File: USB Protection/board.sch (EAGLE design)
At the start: 6 parts

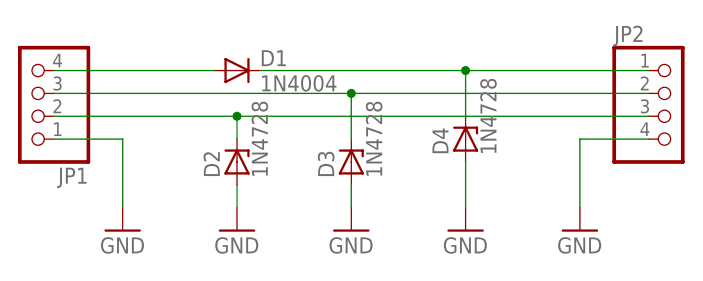
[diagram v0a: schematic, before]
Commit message: Removed power zener diode
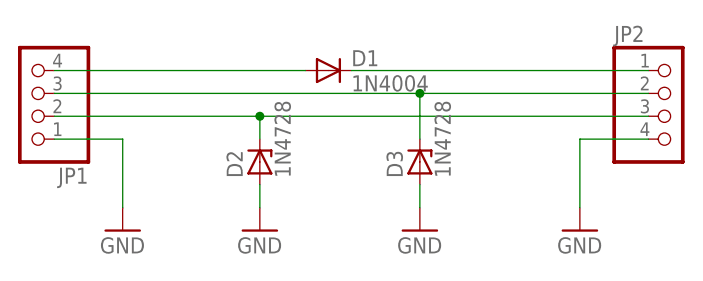
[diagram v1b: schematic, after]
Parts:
- removed D4: 1N4728, diode:1N4728
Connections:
- net GND: no longer D4.A
- net N$2: no longer D4.C
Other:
- moved on the sheet: D1, D2, D3
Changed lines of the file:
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@@
 <part name="D2" library="diode" library_urn="urn:adsk.eagle:library:210" deviceset="1N4728" device="" package3d_urn="urn:adsk.eagle:package:43341/1"/>
 <part name="D3" library="diode" library_urn="urn:adsk.eagle:library:210" deviceset="1N4728" device="" package3d_urn="urn:adsk.eagle:package:43341/1"/>
-<part name="D4" library="diode" library_urn="urn:adsk.eagle:library:210" deviceset="1N4728" device="" package3d_urn="urn:adsk.eagle:package:43341/1"/>
 <part name="JP1" library="pinhead" library_urn="urn:adsk.eagle:library:325" deviceset="PINHD-1X4" device="" package3d_urn="urn:adsk.eagle:package:22407/2"/>
 <part name="JP2" library="pinhead" library_urn="urn:adsk.eagle:library:325" deviceset="PINHD-1X4" device="" package3d_urn="urn:adsk.eagle:package:22407/2"/>
 <part name="GND1" library="supply1" library_urn="urn:adsk.eagle:library:371" deviceset="GND" device=""/>
-<part name="GND2" library="supply1" library_urn="urn:adsk.eagle:library:371" deviceset="GND" device=""/>
 <part name="GND3" library="supply1" library_urn="urn:adsk.eagle:library:371" deviceset="GND" device=""/>
 <part name="GND4" library="supply1" library_urn="urn:adsk.eagle:library:371" deviceset="GND" device=""/>
@@
 </plain>
 <instances>
-<instance part="D1" gate="1" x="10.16" y="55.88"/>
-<instance part="D2" gate="1" x="10.16" y="45.72" rot="R90"/>
-<instance part="D3" gate="1" x="22.86" y="45.72" rot="R90"/>
-<instance part="D4" gate="1" x="35.56" y="48.26" rot="R90"/>
+<instance part="D1" gate="1" x="20.32" y="55.88"/>
+<instance part="D2" gate="1" x="12.7" y="45.72" rot="R90"/>
+<instance part="D3" gate="1" x="30.48" y="45.72" rot="R90"/>
 <instance part="JP1" gate="A" x="-12.7" y="53.34" rot="R180"/>
 <instance part="JP2" gate="A" x="58.42" y="50.8"/>
 <instance part="GND1" gate="1" x="48.26" y="38.1"/>
-<instance part="GND2" gate="1" x="35.56" y="38.1"/>
 <instance part="GND3" gate="1" x="-2.54" y="38.1"/>
-<instance part="GND4" gate="1" x="22.86" y="38.1"/>
-<instance part="GND5" gate="1" x="10.16" y="38.1"/>
+<instance part="GND4" gate="1" x="30.48" y="38.1"/>
+<instance part="GND5" gate="1" x="12.7" y="38.1"/>
 </instances>
 <busses>
@@
 <pinref part="JP1" gate="A" pin="4"/>
 <pinref part="D1" gate="1" pin="A"/>
-<wire x1="-10.16" y1="55.88" x2="7.62" y2="55.88" width="0.1524" layer="91"/>
+<wire x1="-10.16" y1="55.88" x2="17.78" y2="55.88" width="0.1524" layer="91"/>
 </segment>
 </net>
@@
 <pinref part="D1" gate="1" pin="C"/>
 <pinref part="JP2" gate="A" pin="1"/>
-<wire x1="12.7" y1="55.88" x2="35.56" y2="55.88" width="0.1524" layer="91"/>
-<pinref part="D4" gate="1" pin="C"/>
-<wire x1="35.56" y1="55.88" x2="55.88" y2="55.88" width="0.1524" layer="91"/>
-<wire x1="35.56" y1="55.88" x2="35.56" y2="50.8" width="0.1524" layer="91"/>
-<junction x="35.56" y="55.88"/>
+<wire x1="22.86" y1="55.88" x2="55.88" y2="55.88" width="0.1524" layer="91"/>
 </segment>
 </net>
@@
 </segment>
 <segment>
-<pinref part="D4" gate="1" pin="A"/>
-<wire x1="35.56" y1="45.72" x2="35.56" y2="40.64" width="0.1524" layer="91"/>
-<pinref part="GND2" gate="1" pin="GND"/>
-</segment>
-<segment>
 <pinref part="JP1" gate="A" pin="1"/>
 <wire x1="-10.16" y1="48.26" x2="-2.54" y2="48.26" width="0.1524" layer="91"/>
@@
 <pinref part="D2" gate="1" pin="A"/>
 <pinref part="GND5" gate="1" pin="GND"/>
-<wire x1="10.16" y1="43.18" x2="10.16" y2="40.64" width="0.1524" layer="91"/>
+<wire x1="12.7" y1="43.18" x2="12.7" y2="40.64" width="0.1524" layer="91"/>
 </segment>
 <segment>
 <pinref part="D3" gate="1" pin="A"/>
 <pinref part="GND4" gate="1" pin="GND"/>
-<wire x1="22.86" y1="43.18" x2="22.86" y2="40.64" width="0.1524" layer="91"/>
+<wire x1="30.48" y1="43.18" x2="30.48" y2="40.64" width="0.1524" layer="91"/>
 </segment>
 </net>
@@
 <pinref part="JP1" gate="A" pin="3"/>
 <pinref part="JP2" gate="A" pin="2"/>
-<wire x1="-10.16" y1="53.34" x2="22.86" y2="53.34" width="0.1524" layer="91"/>
+<wire x1="-10.16" y1="53.34" x2="30.48" y2="53.34" width="0.1524" layer="91"/>
 <pinref part="D3" gate="1" pin="C"/>
-<wire x1="22.86" y1="53.34" x2="55.88" y2="53.34" width="0.1524" layer="91"/>
-<wire x1="22.86" y1="48.26" x2="22.86" y2="53.34" width="0.1524" layer="91"/>
-<junction x="22.86" y="53.34"/>
+<wire x1="30.48" y1="53.34" x2="55.88" y2="53.34" width="0.1524" layer="91"/>
+<wire x1="30.48" y1="48.26" x2="30.48" y2="53.34" width="0.1524" layer="91"/>
+<junction x="30.48" y="53.34"/>
 </segment>
 </net>
@@
 <pinref part="JP1" gate="A" pin="2"/>
 <pinref part="JP2" gate="A" pin="3"/>
-<wire x1="-10.16" y1="50.8" x2="10.16" y2="50.8" width="0.1524" layer="91"/>
+<wire x1="-10.16" y1="50.8" x2="12.7" y2="50.8" width="0.1524" layer="91"/>
 <pinref part="D2" gate="1" pin="C"/>
-<wire x1="10.16" y1="50.8" x2="55.88" y2="50.8" width="0.1524" layer="91"/>
-<wire x1="10.16" y1="48.26" x2="10.16" y2="50.8" width="0.1524" layer="91"/>
-<junction x="10.16" y="50.8"/>
+<wire x1="12.7" y1="50.8" x2="55.88" y2="50.8" width="0.1524" layer="91"/>
+<wire x1="12.7" y1="48.26" x2="12.7" y2="50.8" width="0.1524" layer="91"/>
+<junction x="12.7" y="50.8"/>
 </segment>
 </net>

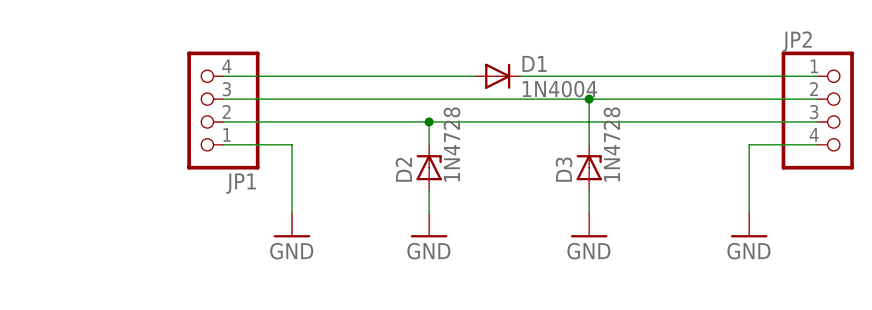
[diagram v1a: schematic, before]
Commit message: Changed to USB port based connection
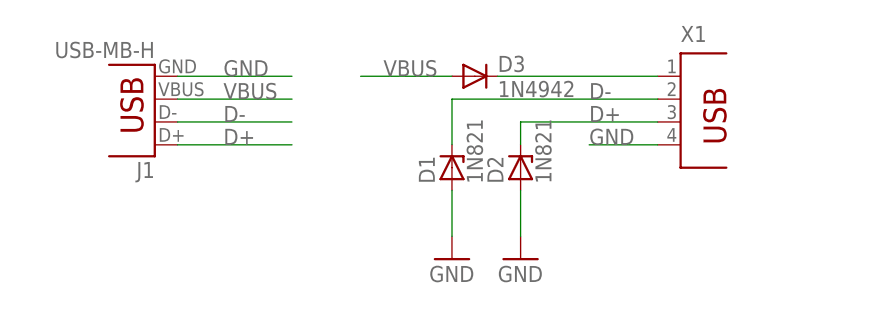
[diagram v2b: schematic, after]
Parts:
- removed JP1, JP2: (no value), pinhead:PINHD-1X4
- added J1: USB-MB-H, SparkFun-Retired:USB-MB-H
- added X1: (no value), con-berg:PN87520
- D1: value 1N4004 -> 1N821; device diode:1N4004 -> diode:1N821
- D2: value 1N4728 -> 1N821; device diode:1N4728 -> diode:1N821
- D3: value 1N4728 -> 1N4942; device diode:1N4728 -> diode:1N4942
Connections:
- removed net N$2: D1.C, JP2.1
- removed net N$3: D2.C, JP1.2, JP2.3
- removed net N$6: D3.C, JP1.3, JP2.2
- new net D+: D2.C, J1.D+, X1.3
- new net D-: D1.C, J1.D-, X1.2
- new net VBUS: D3.A, J1.VBUS
- net GND: now also D1.A, J1.GND, X1.4; no longer D3.A, JP1.1, JP2.4
- net N$1: now also D3.C, X1.1; no longer D1.A, JP1.4
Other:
- moved on the sheet: D2

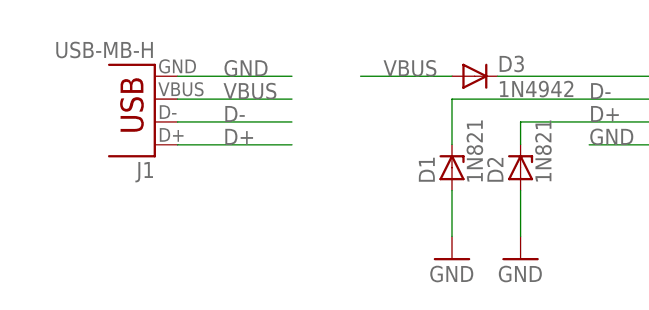
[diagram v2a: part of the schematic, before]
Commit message: Started on base board; made board layout for peripherals
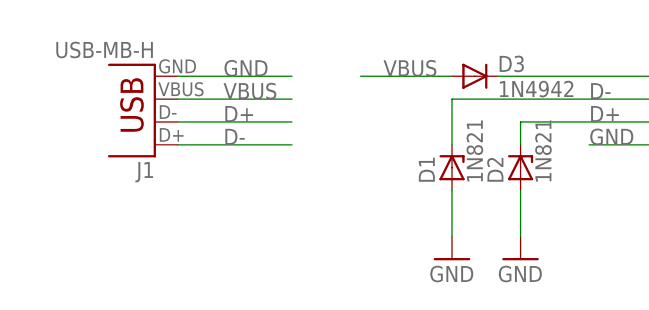
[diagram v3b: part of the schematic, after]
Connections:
- net D+: now also J1.D-; no longer J1.D+
- net D-: now also J1.D+; no longer J1.D-
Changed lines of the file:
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@@
 </segment>
 <segment>
-<pinref part="J1" gate="G$1" pin="D-"/>
-<wire x1="-15.24" y1="50.8" x2="-2.54" y2="50.8" width="0.1524" layer="91"/>
-<label x="-10.16" y="50.8" size="1.778" layer="95"/>
+<pinref part="J1" gate="G$1" pin="D+"/>
+<wire x1="-15.24" y1="48.26" x2="-2.54" y2="48.26" width="0.1524" layer="91"/>
+<label x="-10.16" y="48.26" size="1.778" layer="95"/>
 </segment>
 </net>
@@
 </segment>
 <segment>
-<pinref part="J1" gate="G$1" pin="D+"/>
-<wire x1="-15.24" y1="48.26" x2="-2.54" y2="48.26" width="0.1524" layer="91"/>
-<label x="-10.16" y="48.26" size="1.778" layer="95"/>
+<pinref part="J1" gate="G$1" pin="D-"/>
+<wire x1="-15.24" y1="50.8" x2="-2.54" y2="50.8" width="0.1524" layer="91"/>
+<label x="-10.16" y="50.8" size="1.778" layer="95"/>
 </segment>
 </net>

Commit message: Added lab 6
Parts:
- removed D1, D2: 1N821, diode:1N821
- removed X1: (no value), con-berg:PN87520
- added ENABLE: (no value), pinhead:PINHD-1X2
- added IC1: LM741P, linear:LM741P
- added Q1: (no value), transistor-power:PMOSFET_PTO220BV
- added R1: 560, resistor:R-US_0207/7
- added R2, R3: (no value), resistor:R-US_0207/7
- added USB_A: (no value), con-usb-3:USB-A-H
- D3: value 1N4942 -> BZX55Z2V0; device diode:1N4942 -> diode:1N4148DO35-7
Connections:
- removed net N$1: D3.C, X1.1
- new net VBUS_IN: ENABLE.1, J1.VBUS
- new net VREF: D3.C, IC1.-IN, R1.1
- new net V_EDIV: IC1.+IN, R2.1, R3.2
- new net V_EN: IC1.OUT, Q1.G
- new net V_EXT: Q1.S, R2.2, USB_A.VBUS
- net D+: now also USB_A.D+; no longer D2.C, X1.3
- net D-: now also USB_A.D-; no longer D1.C, X1.2
- net GND: now also D3.A, IC1.V-, R3.1, USB_A.GND; no longer D1.A, D2.A, X1.4
- net VBUS: now also ENABLE.2, IC1.V+, Q1.D, R1.2; no longer D3.A, J1.VBUS
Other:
- moved on the sheet: J1
